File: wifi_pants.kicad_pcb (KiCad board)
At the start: 2 copper layers, 65 x 30 mm, 101 parts, among them P1 CONN_02X20, P2 CONN_01X10, U1 ESP-12E

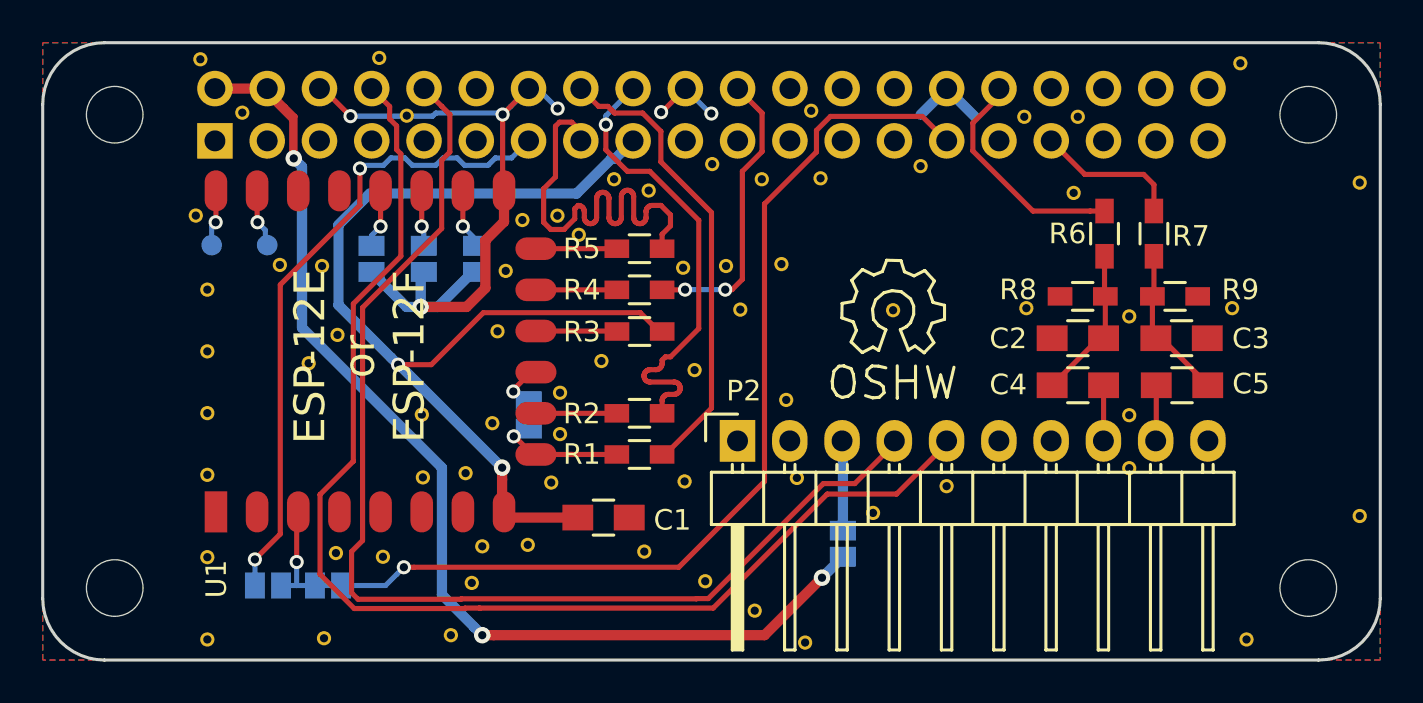
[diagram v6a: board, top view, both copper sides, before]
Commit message: r2 schematic and layout
Changes:
-move module antenna offboard to clear the Pi board and components
-SDIO is now routed over a solid ground plane
-remove test points for UART TX/RX on the module.  these can be
 picked off the module topside
-Default to ID_SD as the CHIP_EN default drive.
-Option for full 4 bit SDIO - no guarantees it works though
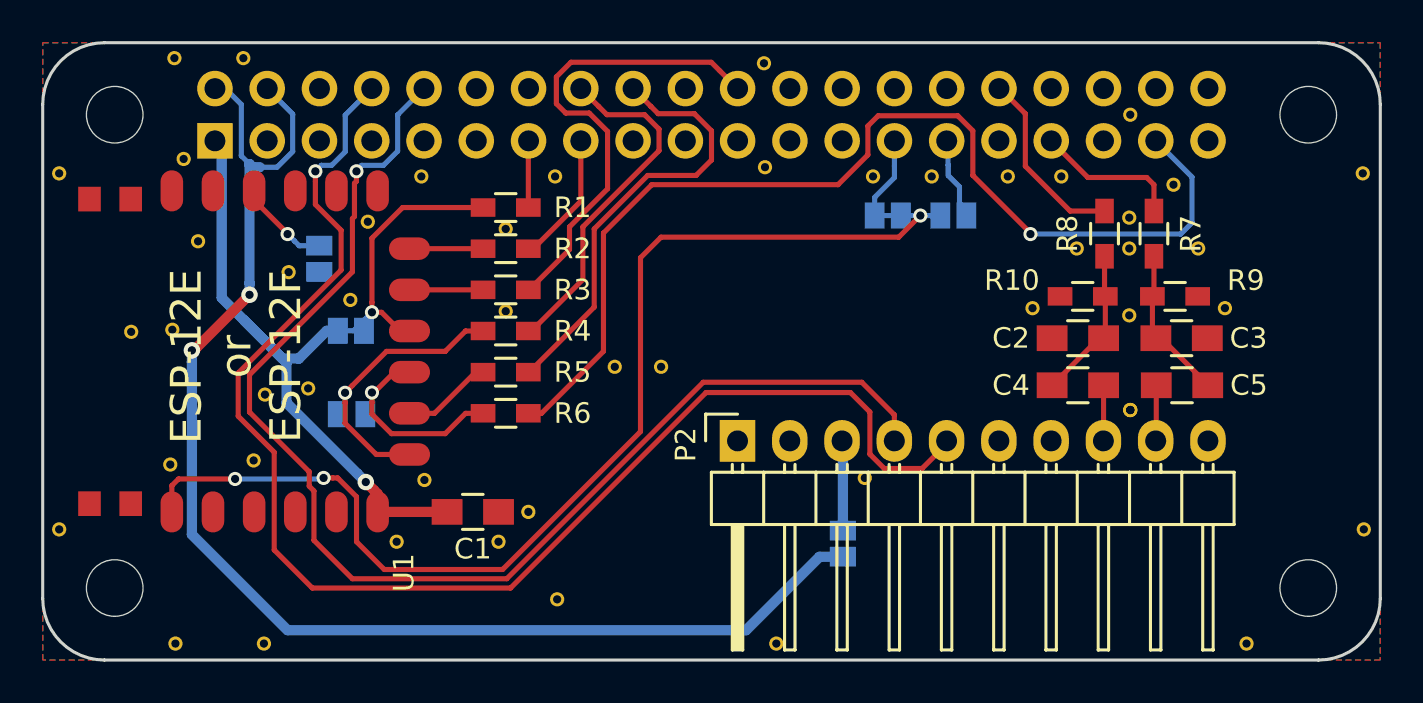
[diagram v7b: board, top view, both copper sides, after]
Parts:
- removed JP4: MTDO, wifi_pants:GS2
- removed the REF** at (79.2, 109.8)
- removed the REF** at (90.1, 104.0)
- removed the REF** at (78.7, 113.9)
- removed the REF** at (87.5, 96.1)
- removed the REF** at (99.6, 112.6)
- removed the REF** at (102.0, 114.2)
- removed the REF** at (123.2, 86.0)
- removed the REF** at (129.0, 91.8)
- removed the REF** at (129.0, 108.0)
- removed the REF** at (123.5, 114.0)
- removed the REF** at (74.7, 88.4)
- removed the REF** at (106.3, 98.0) (x2)
- removed the REF** at (73.0, 97.0)
- removed the REF** at (73.0, 100.0)
- removed the REF** at (73.0, 103.0)
- removed the REF** at (73.0, 106.0)
- removed the REF** at (73.0, 110.0)
- removed the REF** at (73.0, 114.0)
- removed the REF** at (122.8, 97.9)
- removed the REF** at (112.8, 97.9)
- removed the REF** at (115.3, 88.6)
- removed the REF** at (112.7, 88.6)
- removed the REF** at (105.3, 107.8)
- removed the REF** at (115.1, 92.3)
- removed the REF** at (117.8, 103.1)
- removed the REF** at (117.8, 98.3)
- removed the REF** at (85.9, 111.3)
- removed the REF** at (81.5, 110.0)
- removed the REF** at (84.8, 113.8)
- removed the REF** at (101.7, 106.2)
- removed the REF** at (83.4, 103.1)
- removed the REF** at (83.5, 106.1)
- removed the REF** at (86.4, 109.5)
- removed the REF** at (108.9, 106.5)
- removed the REF** at (85.5, 105.9)
- removed the REF** at (77.9, 100.6)
- removed the REF** at (76.5, 95.8)
- removed the REF** at (79.3, 99.2)
- removed the REF** at (100.9, 95.8)
- removed the REF** at (97.2, 111.2)
- removed the REF** at (82.7, 88.5)
- removed the REF** at (78.6, 95.8)
- removed the REF** at (98.9, 98.0)
- removed the REF** at (92.2, 100.5)
- removed the REF** at (117.8, 105.7)
- removed the REF** at (88.6, 109.4)
- removed the REF** at (107.7, 91.0)
- removed the REF** at (102.8, 91.6)
- removed the REF** at (72.7, 85.8)
- removed the REF** at (81.4, 85.7)
- removed the REF** at (102.3, 88.3)
- removed the REF** at (99.9, 91.6)
- removed the REF** at (91.1, 94.3)
- removed the REF** at (94.2, 109.7)
- removed the REF** at (96.2, 106.3)
- removed the REF** at (72.4, 93.4)
- removed the REF** at (89.7, 106.4)
- removed the REF** at (87.1, 99.0)
- removed the REF** at (88.3, 93.6)
- removed the REF** at (96.7, 100.9)
- removed the REF** at (97.5, 90.9)
- removed the REF** at (98.2, 95.9)
- removed the REF** at (94.4, 92.2)
- removed the REF** at (90.0, 93.4)
- removed the REF** at (92.8, 91.6)
- removed the REF** at (96.1, 95.9)
- removed the REF** at (86.8, 103.5)
- removed the REF** at (101.1, 102.4)
- removed the REF** at (90.1, 102.0)
- removed W2, W3, W4: MOUNT, wifi_pants:NPTH_Hole_2_75mm
- removed W5: ESP_TXD, wifi_pants:Measurement_Point_Round-SMD-Pad_Small
- removed W6: ESP_RXD, wifi_pants:Measurement_Point_Round-SMD-Pad_Small
- added R10: 150, Resistors_SMD:R_0603_HandSoldering, F.Cu at (115.5, 97.3)
- added REF**: VIA_0.40mm, wifi_pants:VIA_0.40mm, F.Cu at (123.5, 114.2)
- added REF**: VIA_0.40mm, wifi_pants:VIA_0.40mm, F.Cu at (75.2, 105.3)
- added REF**: VIA_0.40mm, wifi_pants:VIA_0.40mm, F.Cu at (83.4, 91.5)
- added REF**: VIA_0.40mm, wifi_pants:VIA_0.40mm, F.Cu at (89.9, 91.5)
- added REF**: VIA_0.40mm, wifi_pants:VIA_0.40mm, F.Cu at (100.0, 86.0)
- added REF** (x2): VIA_0.40mm, wifi_pants:VIA_0.40mm, F.Cu at (117.8, 102.8)
- added REF**: VIA_0.40mm, wifi_pants:VIA_0.40mm, F.Cu at (105.0, 106.2)
- added REF**: VIA_0.40mm, wifi_pants:VIA_0.40mm, F.Cu at (100.7, 114.2)
- added REF**: VIA_0.40mm, wifi_pants:VIA_0.40mm, F.Cu at (75.8, 114.2)
- added REF**: VIA_0.40mm, wifi_pants:VIA_0.40mm, F.Cu at (71.5, 114.2)
- added REF**: VIA_0.40mm, wifi_pants:VIA_0.40mm, F.Cu at (71.3, 99.0)
- added REF**: VIA_0.40mm, wifi_pants:VIA_0.40mm, F.Cu at (129.2, 91.3)
- added REF**: VIA_0.40mm, wifi_pants:VIA_0.40mm, F.Cu at (71.2, 105.5)
- added REF**: VIA_0.40mm, wifi_pants:VIA_0.40mm, F.Cu at (65.8, 108.7)
- added REF**: VIA_0.40mm, wifi_pants:VIA_0.40mm, F.Cu at (71.4, 85.8)
- added REF**: VIA_0.40mm, wifi_pants:VIA_0.40mm, F.Cu at (72.5, 94.7)
- added REF**: VIA_0.40mm, wifi_pants:VIA_0.40mm, F.Cu at (83.5, 106.2)
- added REF**: VIA_0.40mm, wifi_pants:VIA_0.40mm, F.Cu at (75.8, 102.1)
- added REF**: VIA_0.40mm, wifi_pants:VIA_0.40mm, F.Cu at (82.2, 109.2)
- added REF**: VIA_0.40mm, wifi_pants:VIA_0.40mm, F.Cu at (87.2, 109.2)
- added REF**: VIA_0.40mm, wifi_pants:VIA_0.40mm, F.Cu at (88.6, 107.8)
- added REF**: VIA_0.40mm, wifi_pants:VIA_0.40mm, F.Cu at (77.0, 96.2)
- added REF**: VIA_0.40mm, wifi_pants:VIA_0.40mm, F.Cu at (129.2, 108.7)
- added REF**: VIA_0.40mm, wifi_pants:VIA_0.40mm, F.Cu at (80.0, 97.5)
- added REF**: VIA_0.40mm, wifi_pants:VIA_0.40mm, F.Cu at (77.9, 101.8)
- added REF**: VIA_0.40mm, wifi_pants:VIA_0.40mm, F.Cu at (65.8, 91.3)
- added REF**: VIA_0.40mm, wifi_pants:VIA_0.40mm, F.Cu at (69.3, 99.0)
- added REF**: VIA_0.40mm, wifi_pants:VIA_0.40mm, F.Cu at (87.5, 98.0)
- added REF**: VIA_0.40mm, wifi_pants:VIA_0.40mm, F.Cu at (87.5, 94.0)
- added REF**: VIA_0.40mm, wifi_pants:VIA_0.40mm, F.Cu at (92.8, 100.8)
- added REF**: VIA_0.40mm, wifi_pants:VIA_0.40mm, F.Cu at (122.5, 97.9)
- added REF**: VIA_0.40mm, wifi_pants:VIA_0.40mm, F.Cu at (113.1, 97.9)
- added REF**: VIA_0.40mm, wifi_pants:VIA_0.40mm, F.Cu at (80.8, 93.7)
- added REF**: VIA_0.40mm, wifi_pants:VIA_0.40mm, F.Cu at (117.8, 98.2)
- added REF**: VIA_0.40mm, wifi_pants:VIA_0.40mm, F.Cu at (120.0, 91.9)
- added REF**: VIA_0.40mm, wifi_pants:VIA_0.40mm, F.Cu at (117.8, 88.5)
- added REF**: VIA_0.40mm, wifi_pants:VIA_0.40mm, F.Cu at (121.2, 95.0)
- added REF**: VIA_0.40mm, wifi_pants:VIA_0.40mm, F.Cu at (115.2, 95.0)
- added REF**: VIA_0.40mm, wifi_pants:VIA_0.40mm, F.Cu at (114.5, 91.5)
- added REF**: VIA_0.40mm, wifi_pants:VIA_0.40mm, F.Cu at (111.9, 91.5)
- added REF**: VIA_0.40mm, wifi_pants:VIA_0.40mm, F.Cu at (108.2, 91.5)
- added REF**: VIA_0.40mm, wifi_pants:VIA_0.40mm, F.Cu at (105.3, 91.5)
- added REF**: VIA_0.40mm, wifi_pants:VIA_0.40mm, F.Cu at (117.8, 95.0)
- added REF**: VIA_0.40mm, wifi_pants:VIA_0.40mm, F.Cu at (71.8, 90.7)
- added REF**: VIA_0.40mm, wifi_pants:VIA_0.40mm, F.Cu at (117.8, 93.5)
- added REF**: VIA_0.40mm, wifi_pants:VIA_0.40mm, F.Cu at (74.8, 85.8)
- added REF**: VIA_0.40mm, wifi_pants:VIA_0.40mm, F.Cu at (100.1, 91.0)
- added REF**: VIA_0.40mm, wifi_pants:VIA_0.40mm, F.Cu at (90.0, 112.0)
- added REF**: VIA_0.40mm, wifi_pants:VIA_0.40mm, F.Cu at (95.0, 100.8)
- added W1: MOUNT, wifi_pants:NPTH_Hole_2_75mm, F.Cu at (126.5, 88.5)
- added W1: MOUNT, wifi_pants:NPTH_Hole_2_75mm, F.Cu at (126.5, 111.5)
- added W1: MOUNT, wifi_pants:NPTH_Hole_2_75mm, F.Cu at (68.5, 111.5)
- JP1: value 27 -> GPIO5
- JP2: value 5 -> ID_SD
- JP5: value GPIO2 -> WP_DISABLE
- R1: value 100 -> 150-DNP
- R2, R4, R5: value 100 -> 150
- R3: value 1K -> 150
- R6: value 270 -> 150-DNP
- R8: value 150 -> 270
- moved JP1 37.8 mm to (109.2, 93.4), turned to 90 degrees
- moved JP2 32.6 mm to (106.1, 93.4)
- moved R6 30.4 mm to (87.5, 103.0), turned to 180 degrees
- moved R1 13.6 mm to (87.5, 93.0)
- moved R2 10.3 mm to (87.5, 95.0)
- moved R5 8.85 mm to (87.5, 101.0)
- moved JP3 8.65 mm to (80.0, 103.0), turned to 270 degrees
- moved R3 6.81 mm to (87.5, 97.0)
- moved R4 6.80 mm to (87.5, 99.0)
- moved C1 6.36 mm to (85.9, 107.8)
- moved U1 6.14 mm to (67.3, 108.0)
- moved G*** 5.55 mm to (80.8, 108.8)
- moved JP5 4.98 mm to (80.0, 99.0), turned to 90 degrees
- moved R8 3.23 mm to (116.6, 94.3), turned to 270 degrees
- moved JP6 2.54 mm to (78.4, 95.5)
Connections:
- JP1 pad 1: GPIO27 -> GPIO5
- JP1 pad 2: GPIO5 -> ID_SD
- JP2 pad 1: GPIO5 -> ID_SD
- JP2 pad 2: GPIO5 -> ID_SD
- JP5 pad 1: Net-(JP5-Pad1) -> +3V3
- JP5 pad 2: GND -> +3V3
- P1 pad 1: (no net) -> +3V3
- P1 pad 11: (no net) -> Net-(P1-Pad11)
- P1 pad 12: (no net) -> Net-(P1-Pad12)
- P1 pad 13: GPIO27 -> SD_D3
- P1 pad 17: +3V3 -> Net-(P1-Pad17)
- P1 pad 19: (no net) -> Net-(P1-Pad19)
- P1 pad 21: (no net) -> Net-(P1-Pad21)
- P1 pad 23: (no net) -> Net-(P1-Pad23)
- P1 pad 24: (no net) -> Net-(P1-Pad24)
- P1 pad 26: (no net) -> Net-(P1-Pad26)
- P1 pad 27: (no net) -> ID_SD
- P1 pad 28: (no net) -> Net-(P1-Pad28)
- P1 pad 3: (no net) -> Net-(P1-Pad3)
- P1 pad 31: (no net) -> Net-(P1-Pad31)
- P1 pad 35: (no net) -> Net-(P1-Pad35)
- P1 pad 36: (no net) -> Net-(P1-Pad36)
- P1 pad 37: (no net) -> SD_D2
- P1 pad 38: (no net) -> Net-(P1-Pad38)
- P1 pad 40: (no net) -> Net-(P1-Pad40)
- P1 pad 5: (no net) -> Net-(P1-Pad5)
- P1 pad 7: (no net) -> Net-(P1-Pad7)
- P1 pad 9: (no net) -> Net-(P1-Pad9)
- P2 pad 2: (no net) -> Net-(P2-Pad2)
- P2 pad 6: (no net) -> Net-(P2-Pad6)
- R1 pad 1: SD_CMD -> SD_D3
- R1 pad 2: //CS -> +3V3
- R2 pad 1: SD_D0 -> SD_CLK
- R2 pad 2: /SO -> /CLK
- R3 pad 1: +3V3 -> SD_D1
- R3 pad 2: //WP -> /SI
- R4 pad 1: SD_D1 -> SD_CMD
- R4 pad 2: /SI -> //CS
- R5 pad 1: SD_CLK -> SD_D0
- R5 pad 2: /CLK -> /SO
- R6 pad 1: PWM0_DAC_R -> SD_D2
- R6 pad 2: Net-(C2-Pad2) -> //HOLD
- R8 pad 1: GND -> PWM0_DAC_R
- U1 pad 1: (no net) -> Net-(U1-Pad1)
- U1 pad 12: //WP -> +3V3
- U1 pad 17: Net-(JP5-Pad1) -> Net-(U1-Pad17)
- U1 pad 19: (no net) -> Net-(U1-Pad19)
- U1 pad 2: (no net) -> Net-(U1-Pad2)
- U1 pad 20: (no net) -> Net-(U1-Pad20)
- U1 pad 3: GPIO5 -> ID_SD
- U1 pad 4: (no net) -> Net-(U1-Pad4)
- U1 pad 5: (no net) -> Net-(U1-Pad5)
- U1 pad 6: (no net) -> Net-(U1-Pad6)
- U1 pad 7: (no net) -> Net-(U1-Pad7)
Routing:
- net ID_SD: track 0.00 -> 60.2 mm, vias 0 -> 3
- net GPIO5: track 55.1 -> 4.03 mm, vias 2 -> 0
- net SD_D2: track 0.00 -> 51.0 mm, vias 0 -> 1
- net GND: track 43.4 -> 1.08 mm, vias 6 -> 0
- net GPIO27: track 31.7 -> 0.00 mm, vias 2 -> 0
- net SD_CLK: track 22.5 -> 6.44 mm
- net SD_D1: track 14.3 -> 23.3 mm, vias 2 -> 0
- net +5V: track 56.8 -> 65.0 mm, vias 3 -> 2
- net //HOLD: track 3.13 -> 10.7 mm
- net +3V3: track 52.4 -> 44.9 mm
- net PI_UART0_TXD: track 60.5 -> 67.9 mm, vias 0 -> 1
- net //CS: track 7.26 -> 14.4 mm
- net PI_UART0_RXD: track 56.8 -> 62.4 mm, vias 0 -> 1
- net SD_CMD: track 22.6 -> 17.1 mm
- net //WP: track 3.77 -> 0.00 mm
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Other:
- board text added: "r2"
- board text removed: "r1"

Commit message: start adding boost converter
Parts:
- added REF**: VIA_0.40mm, wifi_pants:VIA_0.40mm, F.Cu at (74.2, 94.5)
- moved REF** 0.76 mm to (71.8, 94.5)
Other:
- rule pad_to_mask_clearance: 0.2 -> 0.07
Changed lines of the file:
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@@
     (tracks 270)
     (zones 0)
-    (modules 79)
+    (modules 80)
     (nets 59)
   )
@@
     (pad_size 0.69 0.69)
     (pad_drill 0.4)
-    (pad_to_mask_clearance 0.2)
+    (pad_to_mask_clearance 0.07)
     (aux_axis_origin 0 0)
     (visible_elements 7FFFFF7F)
@@
   )
   (module wifi_pants:VIA_0.40mm (layer F.Cu)
+    (at 74.2 94.55)
+    (zone_connect 2)
+    (fp_text reference REF** (at 0.4 -4.8) (layer Cmts.User) hide
+      (effects (font (size 1 1) (thickness 0.15)))
+    )
+    (fp_text value VIA_0.40mm (at -0.2 -3.3) (layer Cmts.User) hide
+      (effects (font (size 1 1) (thickness 0.15)))
+    )
+    (pad 1 thru_hole circle (at 0 0) (size 0.69 0.69) (drill 0.4) (layers *.Cu)
+      (net 1 GND) (zone_connect 2))
+  )
+  (module wifi_pants:VIA_0.40mm (layer F.Cu)
     (at 123.5 114.2)
     (zone_connect 2)
@@
   )
   (module wifi_pants:VIA_0.40mm (layer F.Cu)
-    (at 72.55 94.65)
+    (at 71.8 94.55)
     (zone_connect 2)
     (fp_text reference REF** (at 0.4 -4.8) (layer Cmts.User) hide
@@
       (effects (font (size 1 1) (thickness 0.15)) (justify mirror))
     )
-    (fp_text value CONN_02X20 (at -24.13 4.37) (layer B.Fab)
+    (fp_text value CONN_02X20 (at 0 3.6) (layer B.Fab)
       (effects (font (size 1 1) (thickness 0.15)) (justify mirror))
     )
@@
   (segment (start 88.61 87.23) (end 89.051787 87.23) (width 0.25) (layer B.Cu) (net 1) (status 30))
   (segment (start 114.466868 97.454322) (end 114.290028 97.277482) (width 0.25) (layer F.Cu) (net 1) (status 30))
+  (segment (start 73.37 89.77) (end 73.35 89.79) (width 0.5) (layer B.Cu) (net 2))
+  (segment (start 73.35 89.79) (end 73.35 97.05) (width 0.5) (layer B.Cu) (net 2))
+  (segment (start 73.35 97.05) (end 74.8 98.5) (width 0.5) (layer B.Cu) (net 2))
   (segment (start 80.299999 105.950001) (end 80.699998 106.35) (width 0.5) (layer B.Cu) (net 2))
   (segment (start 74.8 98.5) (end 76.85 100.55) (width 0.5) (layer B.Cu) (net 2))
@@
   (segment (start 79.34 99) (end 80.1 99) (width 0.25) (layer B.Cu) (net 2))
   (via (at 81 98.1) (size 0.6858) (drill 0.4) (layers F.Cu B.Cu) (net 2))
-  (segment (start 73.37 89.77) (end 73.7 90.1) (width 0.5) (layer B.Cu) (net 2))
-  (segment (start 73.7 90.1) (end 73.7 97.4) (width 0.5) (layer B.Cu) (net 2))
-  (segment (start 73.7 97.4) (end 74.8 98.5) (width 0.5) (layer B.Cu) (net 2))
   (segment (start 74.8 98.5) (end 76.65 100.35) (width 0.5) (layer B.Cu) (net 2))
   (segment (start 76.65 100.35) (end 77.45 100.35) (width 0.5) (layer B.Cu) (net 2))
